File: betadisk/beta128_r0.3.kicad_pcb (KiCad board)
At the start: 2 copper layers, 99.7 x 149.9 mm, 89 parts, among them J1 ZX_Spectrum_Connector_GENERIC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, J2 Conn_02x17_Odd_Even, Q1 BC639, SW1 SW_DIP_x02, U10 74LS174, U11 74LS367, U12 FDC_MB8877, U13 74LS14, U14 74LS139, U15 74LS06, U16 74LS74, U17 74LS161, U18 74LS161, U19 74LS00, U21 L7805, U22 GAL22V10, U3 W27C512, U4 74LS32, U6 74LS30, U7 74LS123, U8 74LS74, U9 74LS07, U99 74LS245, Y1 8.000Mhz

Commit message: update on libs
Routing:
- net (no net): vias 15 -> 0
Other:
- outline, holes or cut-outs redrawn
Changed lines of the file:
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@@
-(kicad_pcb (version 20200119) (host pcbnew "5.99.0-unknown-4dfe630~86~ubuntu19.10.1")
+(kicad_pcb (version 20200119) (host pcbnew "5.99.0-unknown-51b9944~86~ubuntu19.10.1")
   (general
     (thickness 1.6)
-    (drawings 42)
-    (tracks 2388)
+    (drawings 36)
+    (tracks 2373)
     (modules 89)
     (nets 147)
@@
     (effects (font (size 1.5 1.4) (thickness 0.25)) (justify mirror))
   )
-  (gr_line (start 116.205 170.18) (end 133.985 170.18) (layer "Edge.Cuts") (width 0.1))
-  (gr_line (start 38.1 170.18) (end 83.185 170.18) (layer "Edge.Cuts") (width 0.1))
-  (gr_line (start 123.19 171.45) (end 116.205 171.45) (layer "Edge.Cuts") (width 0.1))
-  (gr_line (start 41.275 171.45) (end 83.185 171.45) (layer "Edge.Cuts") (width 0.1))
-  (gr_line (start 83.185 171.45) (end 83.185 170.18) (layer "Edge.Cuts") (width 0.1))
-  (gr_line (start 116.205 171.45) (end 116.205 170.18) (layer "Edge.Cuts") (width 0.1))
-  (gr_line (start 123.19 184.15) (end 123.19 171.45) (layer "Edge.Cuts") (width 0.1))
+  (gr_line (start 123.19 170.18) (end 129.54 170.18) (layer "Edge.Cuts") (width 0.1))
+  (gr_line (start 38.1 170.18) (end 41.275 170.18) (layer "Edge.Cuts") (width 0.1))
+  (gr_line (start 123.19 184.15) (end 123.19 170.18) (layer "Edge.Cuts") (width 0.1))
   (gr_line (start 106.045 184.15) (end 123.19 184.15) (layer "Edge.Cuts") (width 0.1))
   (gr_line (start 106.045 176.53) (end 106.045 184.15) (layer "Edge.Cuts") (width 0.1))
@@
   (gr_line (start 103.505 184.15) (end 103.505 176.53) (layer "Edge.Cuts") (width 0.1))
   (gr_line (start 41.275 184.15) (end 103.505 184.15) (layer "Edge.Cuts") (width 0.1))
-  (gr_line (start 41.275 171.45) (end 41.275 184.15) (layer "Edge.Cuts") (width 0.1))
+  (gr_line (start 41.275 170.18) (end 41.275 184.15) (layer "Edge.Cuts") (width 0.1))
   (dimension 149.86 (width 0.15) (layer "Dwgs.User")
     (gr_text "149.860 mm" (at 28.54773 109.22 270) (layer "Dwgs.User")
@@
   )
   (gr_line (start 137.795 170.18) (end 137.795 171.45) (layer "Edge.Cuts") (width 0.1))
-  (gr_line (start 133.985 171.45) (end 133.985 170.18) (layer "Edge.Cuts") (width 0.1))
-  (gr_line (start 129.54 171.45) (end 133.985 171.45) (layer "Edge.Cuts") (width 0.1))
   (gr_line (start 137.795 179.07) (end 137.795 171.45) (layer "Edge.Cuts") (width 0.1))
-  (gr_line (start 129.54 179.07) (end 129.54 171.45) (layer "Edge.Cuts") (width 0.1))
+  (gr_line (start 129.54 179.07) (end 129.54 170.18) (layer "Edge.Cuts") (width 0.1))
   (gr_line (start 137.795 179.07) (end 129.54 179.07) (layer "Edge.Cuts") (width 0.1))
   (gr_text "1-2 = Ext\n2-3 = Int" (at 130.81 164.465 90) (layer "F.SilkS")
@@
   (segment (start 72.480001 127.605801) (end 72.480001 133.559101) (width 0.25) (layer "F.Cu") (net 67))
   (segment (start 72.480001 133.559101) (end 72.6465 133.7256) (width 0.25) (layer "F.Cu") (net 67))
-  (via (at 84.455 170.815) (size 0.9) (drill 0.8) (layers "F.Cu" "B.Cu") (net 0))
-  (via (at 86.995 170.815) (size 0.9) (drill 0.8) (layers "F.Cu" "B.Cu") (net 0))
-  (via (at 89.535 170.815) (size 0.9) (drill 0.8) (layers "F.Cu" "B.Cu") (net 0))
-  (via (at 92.075 170.815) (size 0.9) (drill 0.8) (layers "F.Cu" "B.Cu") (net 0))
-  (via (at 94.615 170.815) (size 0.9) (drill 0.8) (layers "F.Cu" "B.Cu") (net 0))
-  (via (at 97.155 170.815) (size 0.9) (drill 0.8) (layers "F.Cu" "B.Cu") (net 0))
-  (via (at 99.695 170.815) (size 0.9) (drill 0.8) (layers "F.Cu" "B.Cu") (net 0))
-  (via (at 114.935 170.815) (size 0.9) (drill 0.8) (layers "F.Cu" "B.Cu") (net 0))
-  (via (at 112.395 170.815) (size 0.9) (drill 0.8) (layers "F.Cu" "B.Cu") (net 0))
-  (via (at 109.855 170.815) (size 0.9) (drill 0.8) (layers "F.Cu" "B.Cu") (net 0))
-  (via (at 102.235 170.815) (size 0.9) (drill 0.8) (layers "F.Cu" "B.Cu") (net 0))
-  (via (at 107.315 170.815) (size 0.9) (drill 0.8) (layers "F.Cu" "B.Cu") (net 0))
-  (via (at 106.045 170.815) (size 0.9) (drill 0.8) (layers "F.Cu" "B.Cu") (net 0))
-  (via (at 104.775 170.815) (size 0.9) (drill 0.8) (layers "F.Cu" "B.Cu") (net 0))
-  (via (at 103.505 170.815) (size 0.9) (drill 0.8) (layers "F.Cu" "B.Cu") (net 0))
   (segment (start 109.22 95.885) (end 109.22 100.965) (width 0.25) (layer "F.Cu") (net 73))
   (segment (start 106.045 104.14) (end 109.22 100.965) (width 0.25) (layer "F.Cu") (net 73))

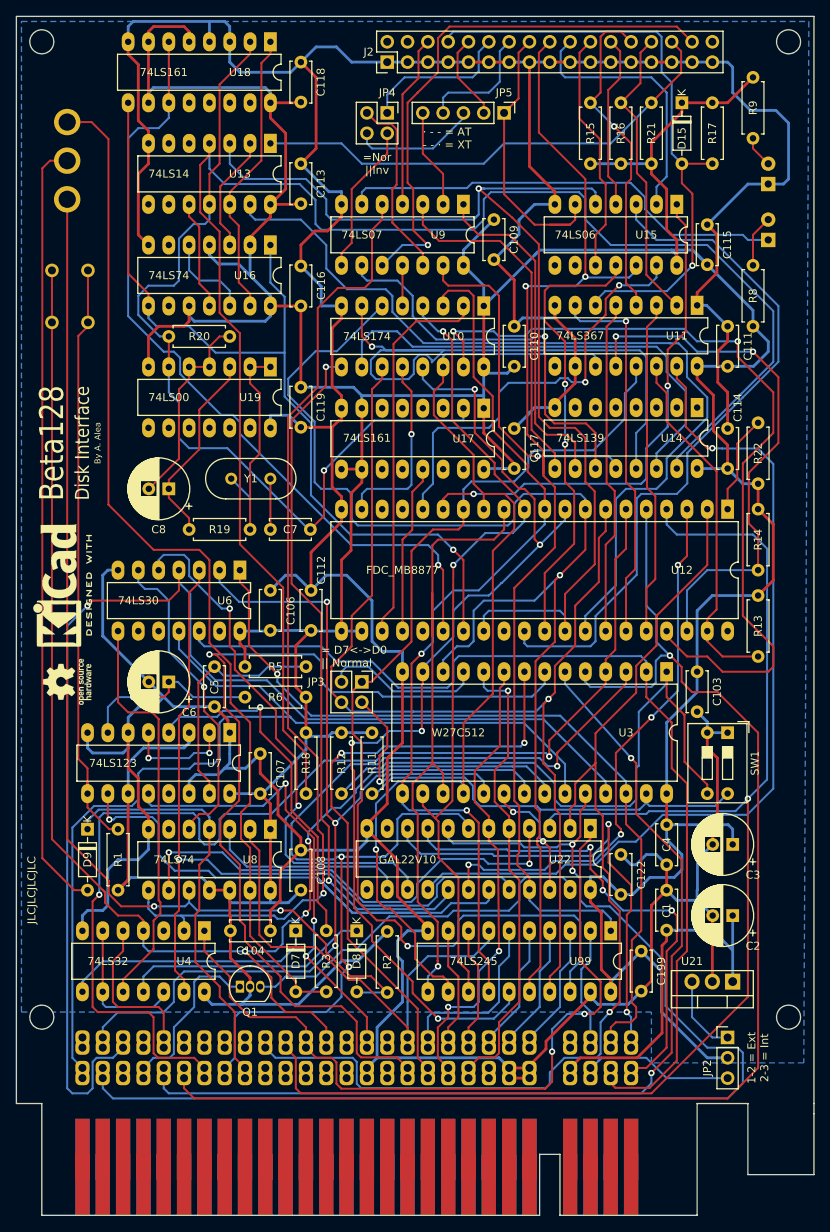
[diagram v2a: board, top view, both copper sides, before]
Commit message: fix duplicate_label
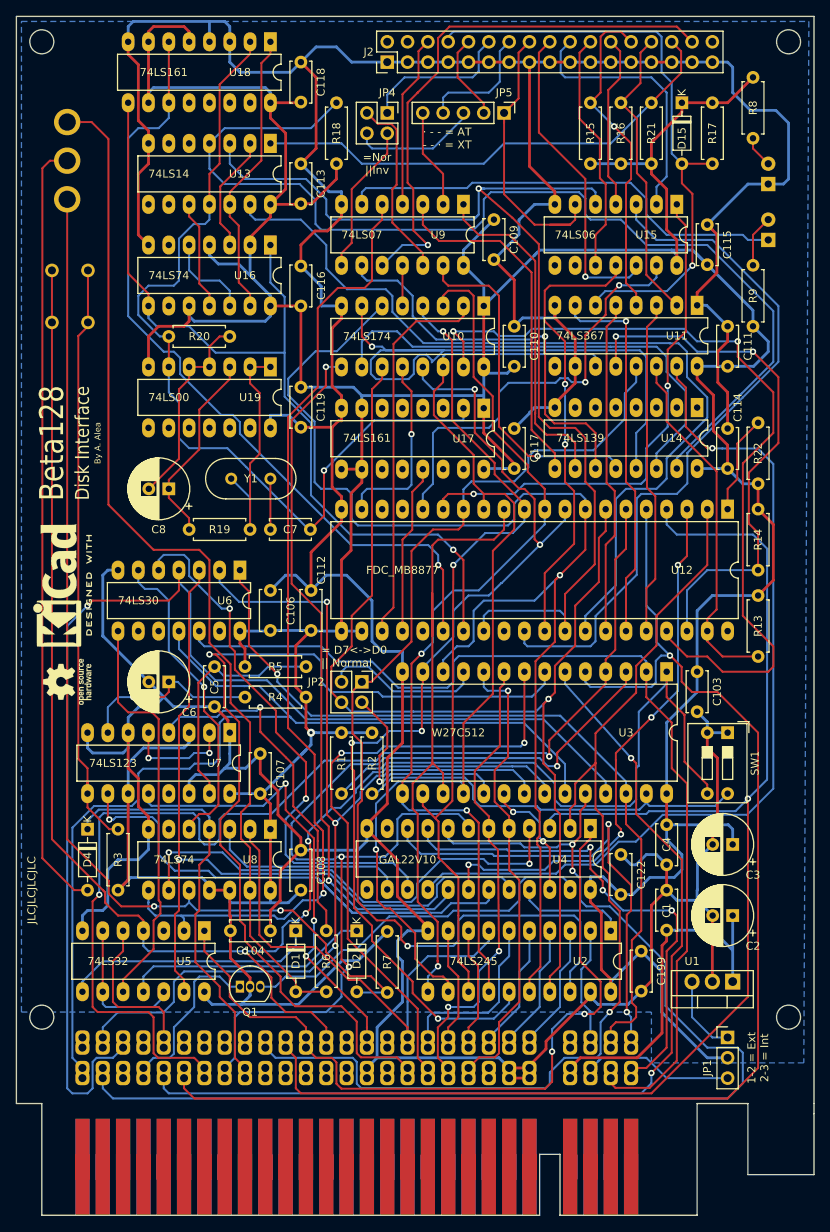
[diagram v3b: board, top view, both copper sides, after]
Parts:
- D15: value BAT42 -> 1N4148
- R13, R14: value 470 -> 10K
- R15, R16, R17: value 470 -> 1K
- moved R18 86.4 mm to (78.1, 45.1), turned to -90 degrees
- renumbered D7 to D1, D8 to D2, D5 to D3, D9 to D4, D1 to D5, JP2 to JP1, JP3 to JP2, R12 to R1, R11 to R2, R1 to R3, R6 to R4, R3 to R6, R2 to R7, R9 to R8, R8 to R9, S2 to S1, S1 to S2, U21 to U1, U99 to U2, U22 to U4, U4 to U5
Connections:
- net /A0 renamed A0
- net /A1 renamed A1
- net /A10 renamed A10
- net /A11 renamed A11
- net /A12 renamed A12
- net /A13 renamed A13
- net /A14 renamed A14
- net /A15 renamed A15
- net /A2 renamed A2
- net /A3 renamed A3
- net /A4 renamed A4
- net /A5 renamed A5
- net /A6 renamed A6
- net /A7 renamed A7
- net /A8 renamed A8
- net /A9 renamed A9
- net /D'0 renamed D'0
- net /D'1 renamed D'1
- net /D'2 renamed D'2
- net /D'3 renamed D'3
- net /D'4 renamed D'4
- net /D'5 renamed D'5
- net /D'6 renamed D'6
- net /D'7 renamed D'7
- net /D0 renamed /Memory Paging Logic/D0
- net /D1 renamed /Memory Paging Logic/D1
- net /D2 renamed /Memory Paging Logic/D2
- net /D3 renamed /Memory Paging Logic/D3
- net /D4 renamed /Memory Paging Logic/D4
- net /D5 renamed /Memory Paging Logic/D5
- net /D6 renamed /Memory Paging Logic/D6
- net /D7 renamed /Memory Paging Logic/D7
- net /MOTOR_ON renamed /Disc Controler Logic/MOTOR_ON
- net /STEP renamed /Disc Controler Logic/STEP
- net /U8B_Q renamed /Memory Paging Logic/BETA_ON
- net //IORQ renamed /Memory Paging Logic//IORQ
- net //M1 renamed /Memory Paging Logic//M1
- net //MREQ renamed /Memory Paging Logic//MREQ
- net //NMI renamed /Memory Paging Logic//NMI
- net //RD renamed /RD
- net //RESET renamed /Memory Paging Logic//RESET
- net //ROMCS renamed /Memory Paging Logic//ROMCS
- net //WR renamed /WR
- net 4Mhz renamed /Disc Controler Logic/8Mhz
- net DATA_READ renamed /Disc Controler Logic/DATA_READ
- net DRQ renamed /Disc Controler Logic/DRQ
- net DS0 renamed /Disc Controler Logic/DS0
- net DS1 renamed /Disc Controler Logic/DS1
- net DS2 renamed /Disc Controler Logic/DS2
- net DS3 renamed /Disc Controler Logic/DS3
- net FDC_IP renamed /Disc Controler Logic/FDC_IP
- net FDC_TR00 renamed /Disc Controler Logic/FDC_TR00
- net FDC_WPRT renamed /Disc Controler Logic/FDC_WPRT
- net FD_CLK renamed /Disc Controler Logic/FD_CLK
- net FD_DATA renamed /Disc Controler Logic/FD_DATA
- net HEAD renamed /Disc Controler Logic/HEAD
- net INTRQ renamed /Disc Controler Logic/INTRQ
- net IO_WR1 renamed /Memory Paging Logic/IO_WR1
- net Net-(R3-Pad1) renamed /Memory Paging Logic//RAMCOPY
- net Net-(U12-Pad24) renamed /Disc Controler Logic/2Mhz
- net Net-(U4-Pad2) renamed /Memory Paging Logic/BLOQ_IO
- net /(A14+A15) renamed /Memory Paging Logic//P123
- net /A9 renamed /Memory Paging Logic//A9
- net /IP renamed /Disc Controler Logic//IP
- net /ROM_CE renamed /Memory Paging Logic//ROM_CE
- net /TR00 renamed /Disc Controler Logic//TR00
- net /WF renamed /Disc Controler Logic//WF
- net /WPRT renamed /Disc Controler Logic//WPRT
- J2 pad 18: DIR -> /Disc Controler Logic/H_DIR
- U15 pad 12: DIR -> /Disc Controler Logic/H_DIR
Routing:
- net DIR: track 144.2 -> 14.0 mm, vias 2 -> 0
- net Net-(R18-Pad1): track 201.6 -> 132.0 mm
- net /Disc Controler Logic/H_DIR: track 0.00 -> 39.7 mm, vias 0 -> 1
- net +5V: track 630.9 -> 639.4 mm, vias 0 -> 1
- net /Memory Paging Logic//A9: track 67.3 -> 68.1 mm

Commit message: fix 74ls00 power pins
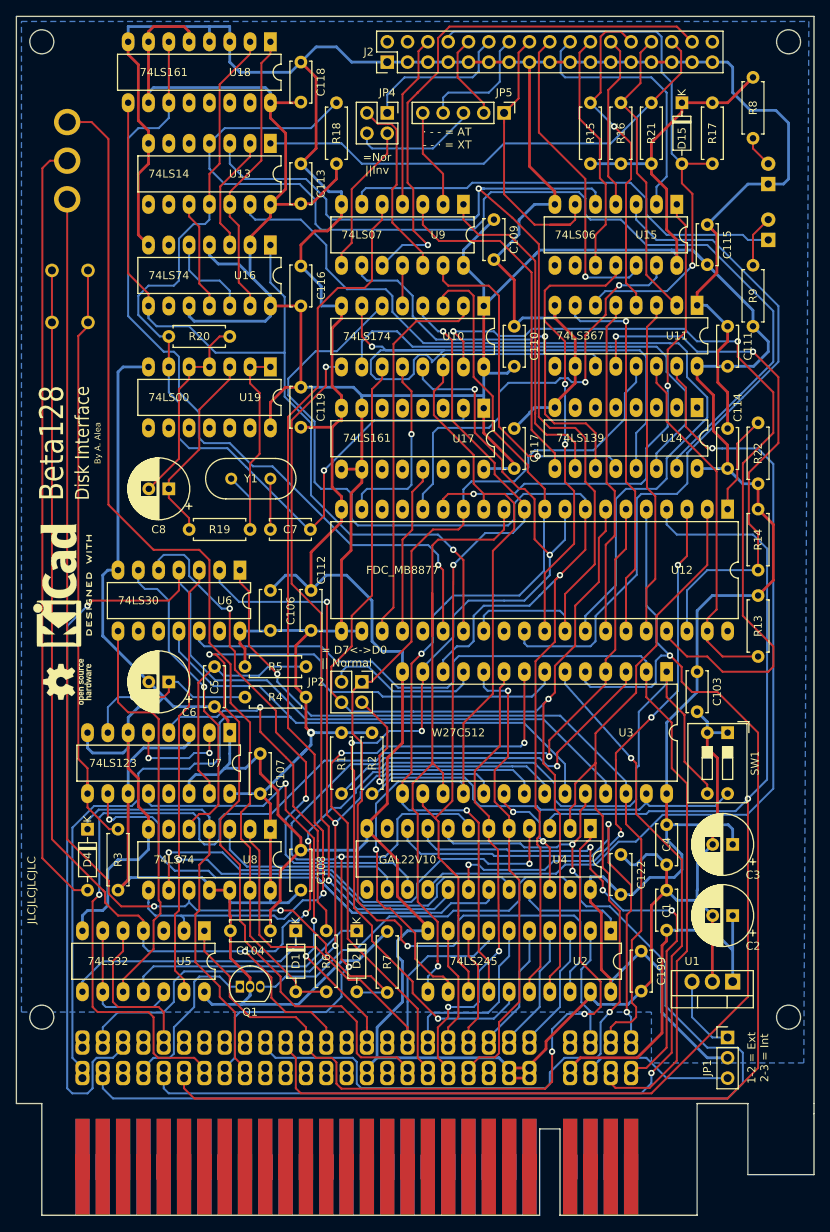
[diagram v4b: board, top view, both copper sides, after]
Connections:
- net /Disc Controler Logic//IP renamed /Disc Controler Logic//IP
- net /Disc Controler Logic//TR00 renamed /Disc Controler Logic//TR00
- net /Disc Controler Logic//WF renamed /Disc Controler Logic//WF
- net /Disc Controler Logic//WPRT renamed /Disc Controler Logic//WPRT
- net /Memory Paging Logic//A9 renamed /Memory Paging Logic//A9
- net /Memory Paging Logic//IORQ renamed /Memory Paging Logic//IORQ
- net /Memory Paging Logic//M1 renamed /Memory Paging Logic//M1
- net /Memory Paging Logic//MREQ renamed /Memory Paging Logic//MREQ
- net /Memory Paging Logic//NMI renamed /Memory Paging Logic//NMI
- net /Memory Paging Logic//P123 renamed /Memory Paging Logic//P123
- net /Memory Paging Logic//RAMCOPY renamed /Memory Paging Logic//RAMCOPY
- net /Memory Paging Logic//RESET renamed /Memory Paging Logic//RESET
- net /Memory Paging Logic//ROMCS renamed /Memory Paging Logic//ROMCS
- net /Memory Paging Logic//ROM_CE renamed /Memory Paging Logic//ROM_CE
- net A14+A15 renamed /Memory Paging Logic//P0
- net DIR renamed /Memory Paging Logic/DIR
- net /RD renamed /RD
- net /WR renamed /WR
- U19 pad 14: GND -> +5V
- U19 pad 7: +5V -> GND
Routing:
- net GND: track 666.1 -> 687.8 mm
- net D'2: track 127.8 -> 132.1 mm
- net +5V: track 639.4 -> 635.6 mm
- net D'3: track 114.2 -> 117.2 mm
- net /Disc Controler Logic/FD_CLK: track 100.8 -> 103.2 mm
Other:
- outline, holes or cut-outs redrawn
